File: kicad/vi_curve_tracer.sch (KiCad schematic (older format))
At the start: 64 parts, among them P1 CONN_01X05, P2 USB_OTG, P3 CONN_01X06, P4 CONN_01X06, P5 CONN_01X02, U1 MCP6004, U2 pic24f08km202, U3 ft230x

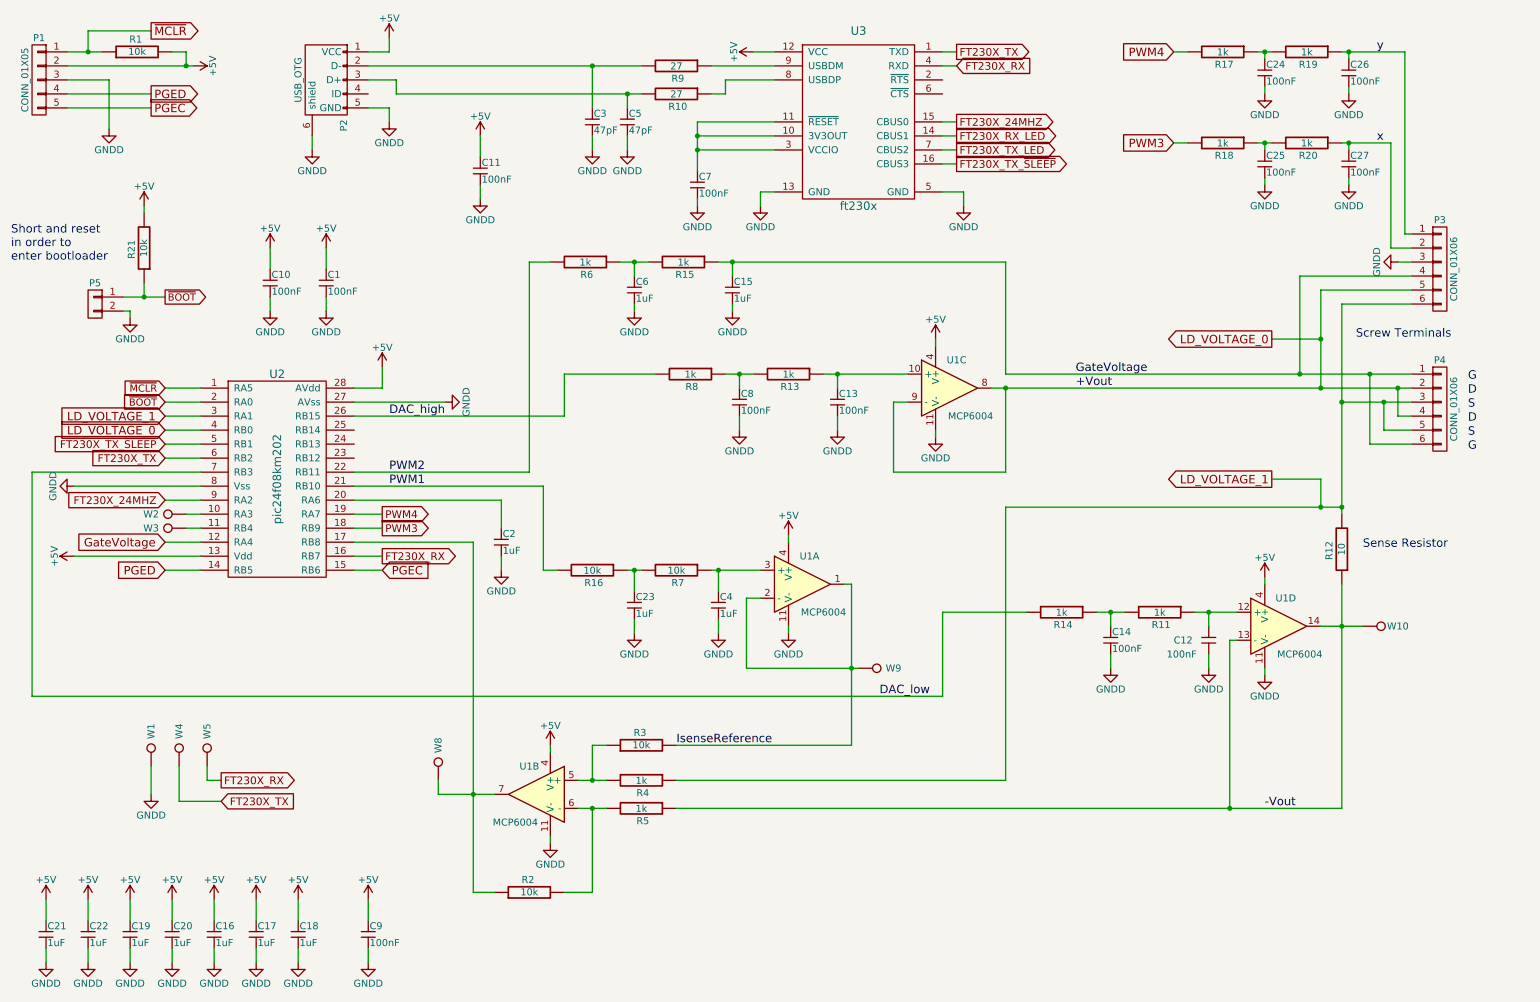
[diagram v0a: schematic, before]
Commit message: Added safety (multimeter) probes for maximimum compatiblity with likely components that the user already has
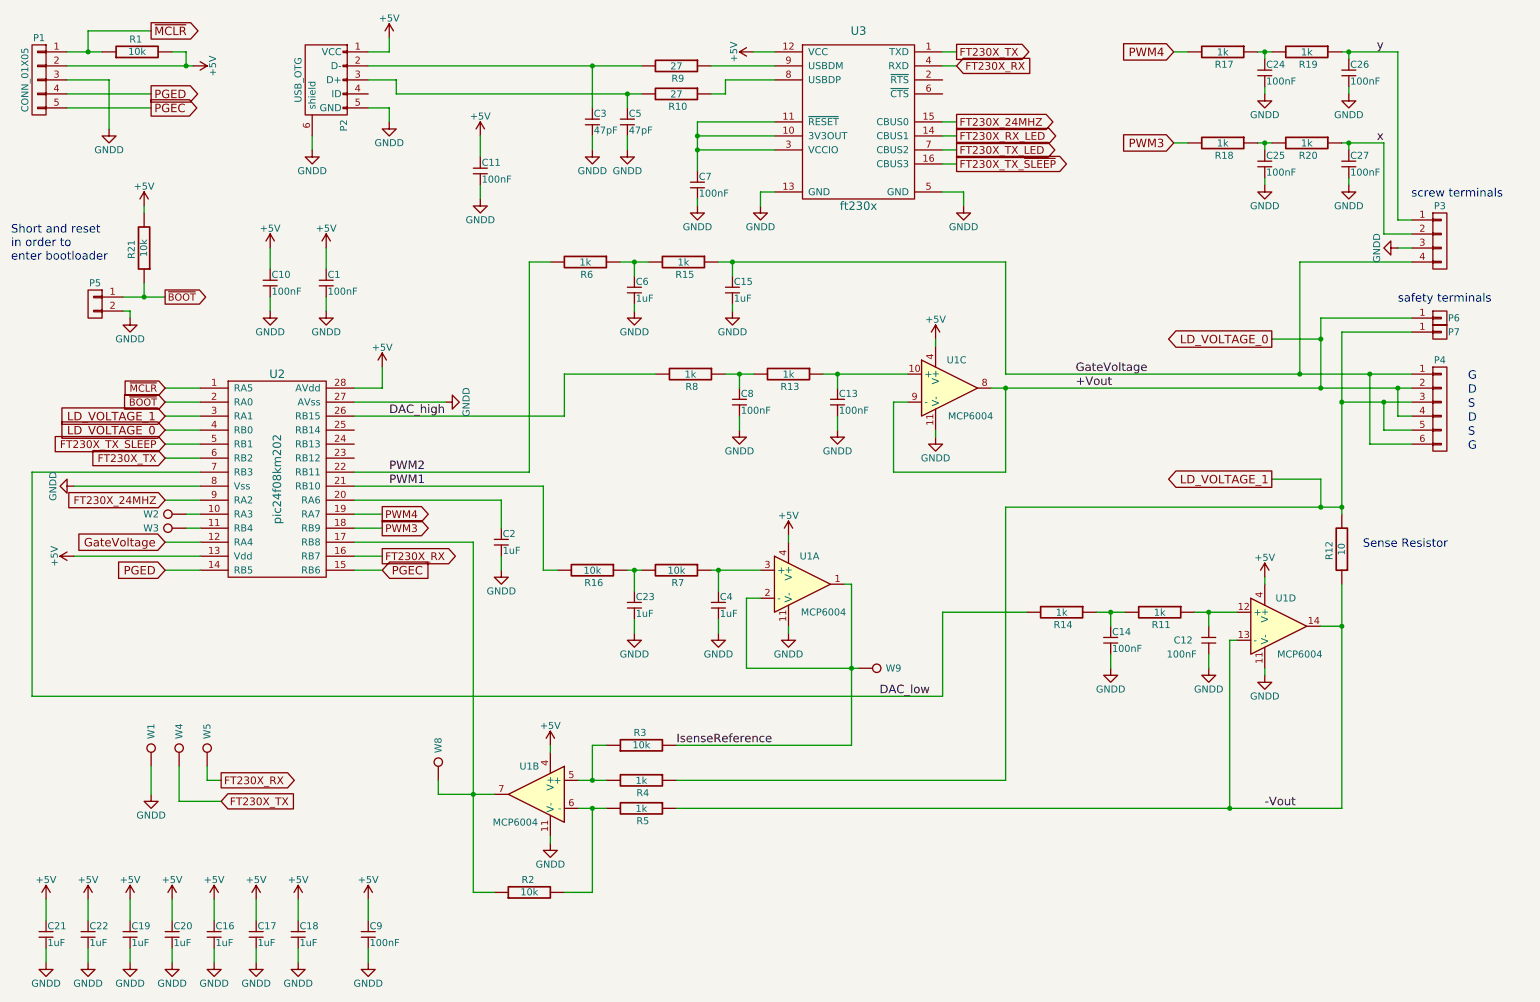
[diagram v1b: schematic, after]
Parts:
- removed P3: CONN_01X06, kicad_pcb:CONN_1x6_OSTTC062162, symbol CONN_01X06
- removed W10: TEST_1P, Measurement_Points:Measurement_Point_Round-SMD-Pad_Small, symbol TEST_1P
- added P3: CONN_01X04, kicad_pcb:CONN_1x4_OSTTC042162, symbol CONN_01X04
- added P6, P7: CONN_01X01, kicad_pcb:CONN_1x1_CT3150, symbol CONN_01X01
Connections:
- net GNDD: now also P3.3 (P3)
- net GateVoltage: now also P3.4 (P4)
- net LD_VOLTAGE_0: now also P6.1 (P1)
- net LD_VOLTAGE_1: now also P7.1 (P1)
- net x: now also P3.2 (P2)
- net y: now also P3.1 (P1)
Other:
- note added: "safety terminals"
- note added: "screw terminals"
- note removed: "Screw Terminals"

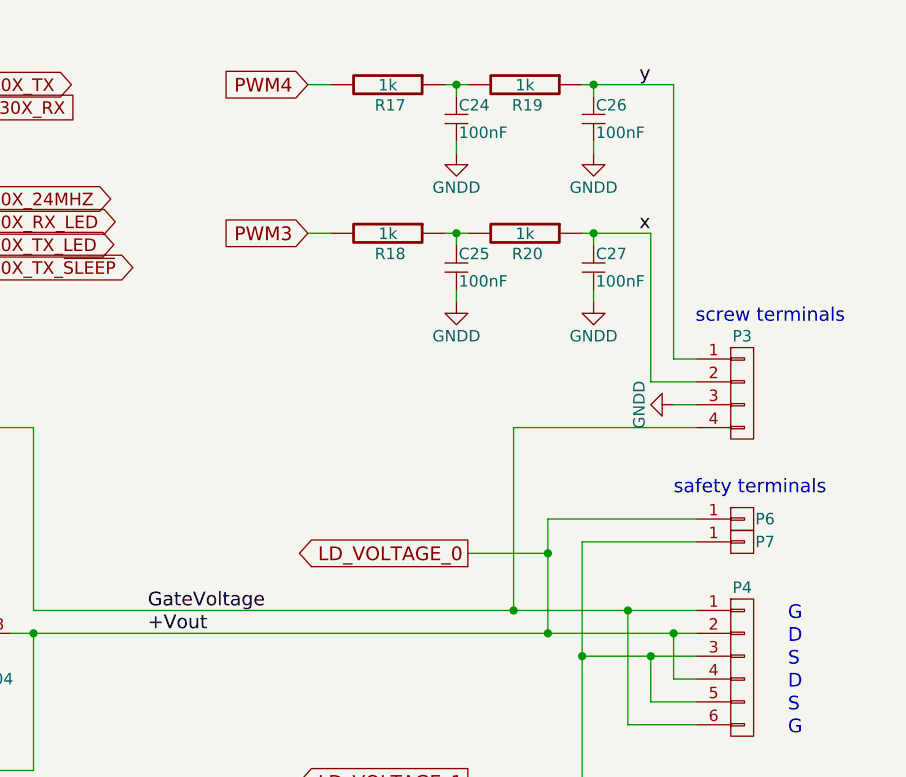
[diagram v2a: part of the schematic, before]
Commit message: Added features to allow connecting to oscilloscope easier, no change to function.
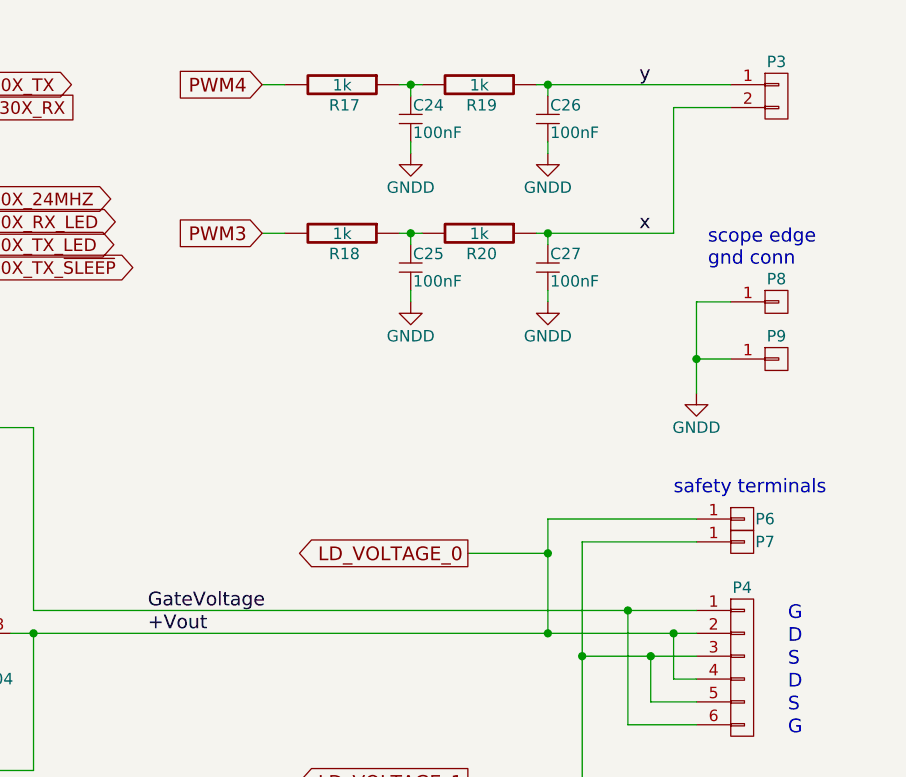
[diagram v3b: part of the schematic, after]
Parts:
- removed P3: CONN_01X04, kicad_pcb:CONN_1x4_OSTTC042162, symbol CONN_01X04
- added P3: CONN_01X02, lib_pcb:CON_1x2_0.1in, symbol CONN_01X02
- added P8, P9: CONN_01X01, lib_pcb:CONN_1x1_EDGE_SCOPE_GND, symbol CONN_01X01
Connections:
- net GNDD: now also P8.1 (P1), P9.1 (P1)
- net x: now also P3.2 (P2)
- net y: now also P3.1 (P1)
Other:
- note added: "scope edge\ngnd conn"
- note removed: "screw terminals"
- moved on the sheet: C24, C25, C26, C27, R17, R18, R19, R20

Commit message: Fixed BOM issue
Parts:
- U1: PN (none) -> ELOAMC6L0400A
- U2: MPN PIC24FV16KM202-I/SO -> PIC24FV16KM202-I/SS
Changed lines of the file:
@@
 F 3 "" H 2450 3950 60  0000 C CNN
 F 4 "Microchip, Inc." H 2450 3950 60  0001 C CNN "Manufacturer"
-F 5 "PIC24FV16KM202-I/SO" H 2450 3950 60  0001 C CNN "MPN"
+F 5 "PIC24FV16KM202-I/SS" H 2450 3950 60  0001 C CNN "MPN"
 F 6 "Microcontroller" H 2450 3950 60  0001 C CNN "Description"
 	1    2450 3950
@@
 F 5 "Opamp 1MHz, Quad, TSSOP-14" H 6200 4700 60  0001 C CNN "Description"
 F 6 "Microchip" H 6200 4700 60  0001 C CNN "Manufacturer"
+F 7 "ELOAMC6L0400A" H 6200 4700 60  0001 C CNN "PN"
 	1    6200 4700
 	1    0    0    -1
@@
 F 5 "Microchip" H 7250 3300 60  0001 C CNN "Manufacturer"
 F 6 "Opamp 1MHz, Quad, TSSOP-14" H 7250 3300 60  0001 C CNN "Description"
+F 7 "ELOAMC6L0400A" H 7250 3300 60  0001 C CNN "PN"
 	3    7250 3300
 	1    0    0    -1
@@
 F 5 "Opamp 1MHz, Quad, TSSOP-14" H 9600 5000 60  0001 C CNN "Description"
 F 6 "Microchip" H 9600 5000 60  0001 C CNN "Manufacturer"
+F 7 "ELOAMC6L0400A" H 9600 5000 60  0001 C CNN "PN"
 	4    9600 5000
 	1    0    0    -1
@@
 F 5 "Opamp 1MHz, Quad, TSSOP-14" H 4300 6200 60  0001 C CNN "Description"
 F 6 "Microchip" H 4300 6200 60  0001 C CNN "Manufacturer"
+F 7 "ELOAMC6L0400A" H 4300 6200 60  0001 C CNN "PN"
 	2    4300 6200
 	-1   0    0    -1
